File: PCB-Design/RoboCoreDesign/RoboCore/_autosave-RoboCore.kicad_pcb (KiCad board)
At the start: 4 copper layers, 68 x 60 mm, 80 parts, among them IC1 DRV8245SQRXZRQ1, IC2 DRV8245SQRXZRQ1, J1 SS-52400-002, J2 B2B-PH-SM4-TB, J3 MOTOR_A, J4 MOTOR_B, Q1 BC817, Q2 BC817, SW1 RESET, SW2 BOOT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

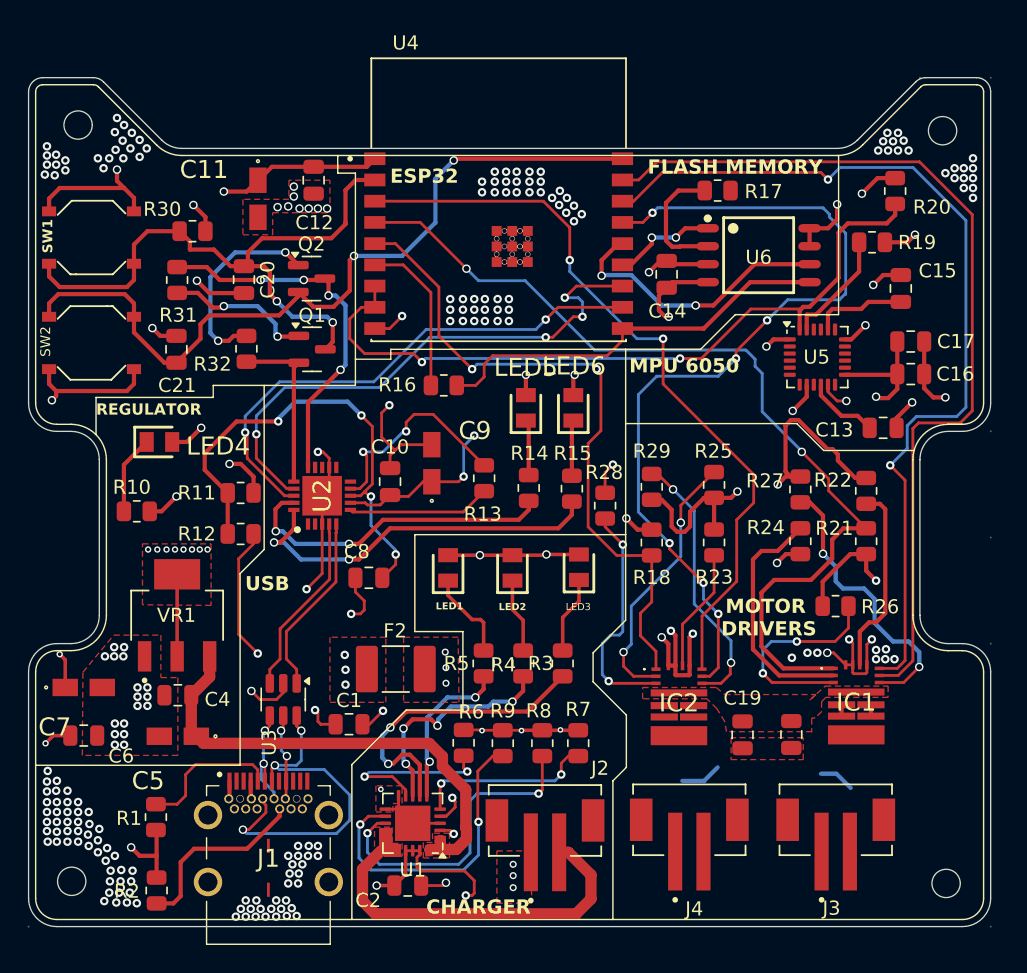
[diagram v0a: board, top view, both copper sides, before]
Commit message: made improvements to the motor copper power, signal planes
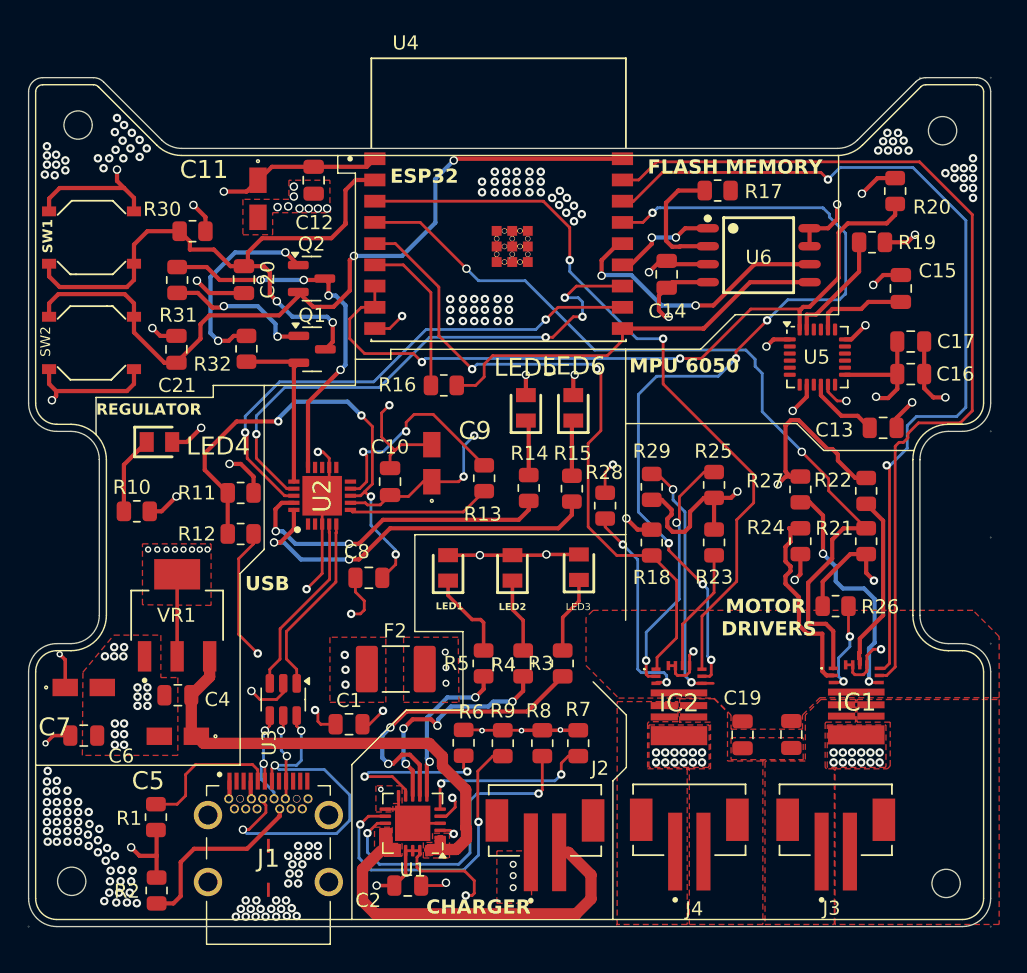
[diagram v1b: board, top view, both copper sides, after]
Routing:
- net GND: track 159.8 -> 150.4 mm, vias 236 -> 248
- net Net-(IC1-NSLEEP): track 15.1 -> 6.60 mm
- net /ESP32_BOARD_CONNECTION/nFAULT_A: track 65.7 -> 60.1 mm
- net Net-(IC1-DRVOFF): track 20.3 -> 17.0 mm
- net /ESP32_BOARD_CONNECTION/MotorDriver/AO2: track 3.21 -> 0.00 mm
- net Net-(IC1-IPROPI): track 17.1 -> 14.0 mm
- net /ESP32_BOARD_CONNECTION/MotorDriver/BO2: track 2.89 -> 0.00 mm
- net Net-(IC2-NSLEEP): track 16.6 -> 15.1 mm
- net Net-(IC2-DRVOFF): track 19.0 -> 17.7 mm
- net Net-(IC2-IPROPI): track 19.0 -> 17.8 mm
- net /ESP32_BOARD_CONNECTION/DIR_A: track 64.7 -> 63.6 mm
- net Net-(IC1-SR): track 13.5 -> 12.6 mm
- net /ESP32_BOARD_CONNECTION/MotorDriver/AO1: track 0.70 -> 0.00 mm
- net /ESP32_BOARD_CONNECTION/nFAULT_B: track 47.5 -> 48.0 mm
- added copper zone on F.Cu, net /ESP32_BOARD_CONNECTION/MotorDriver/AO1
- added copper zone on F.Cu, net /ESP32_BOARD_CONNECTION/MotorDriver/AO2
- added copper zone on F.Cu, net /ESP32_BOARD_CONNECTION/MotorDriver/BO1
- added copper zone on F.Cu, net /ESP32_BOARD_CONNECTION/MotorDriver/BO2
